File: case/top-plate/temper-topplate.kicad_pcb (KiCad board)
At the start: 2 copper layers, 111.4 x 90 mm, 21 parts, among them SW10 SW_PUSH, SW11 SW_PUSH, SW12 SW_PUSH, SW14 SW_PUSH, SW15 SW_PUSH, SW16 SW_PUSH, SW17 SW_PUSH, SW18 SW_PUSH, SW19 SW_PUSH, SW2 SW_PUSH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

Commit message: fix: save plate modification
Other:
- rule pad_to_mask_clearance: 0.2 -> 0
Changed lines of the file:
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@@
 			(dielectric_constraints no)
 		)
-		(pad_to_mask_clearance 0.2)
-		(solder_mask_min_width 0.1)
+		(pad_to_mask_clearance 0)
 		(allow_soldermask_bridges_in_footprints no)
 		(aux_axis_origin 145.73 12.66)
@@
 			(psnegative no)
 			(psa4output no)
-			(plotreference yes)
-			(plotvalue yes)
-			(plotfptext yes)
+			(plotreference no)
+			(plotvalue no)
+			(plotfptext no)
 			(plotinvisibletext no)
 			(sketchpadsonfab no)

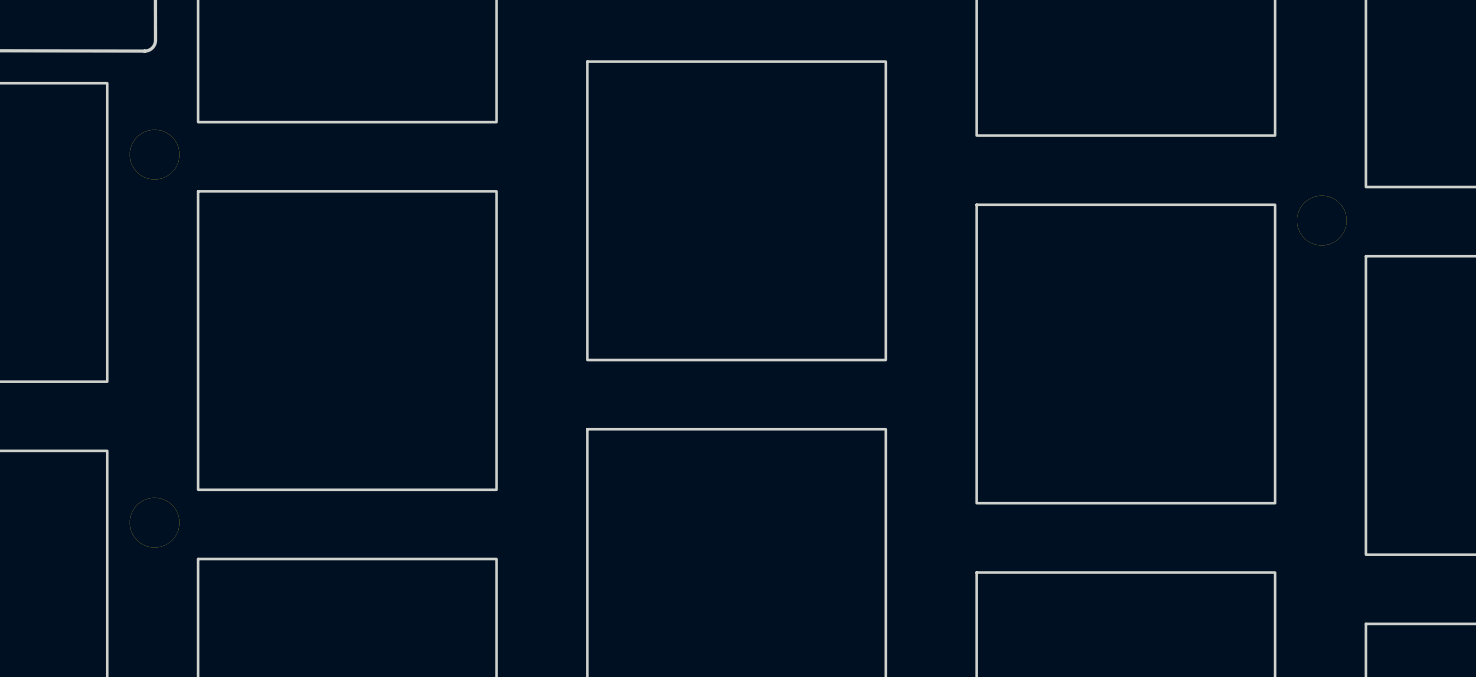
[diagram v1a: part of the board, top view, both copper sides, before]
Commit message: feat: remove useless holes from top plate
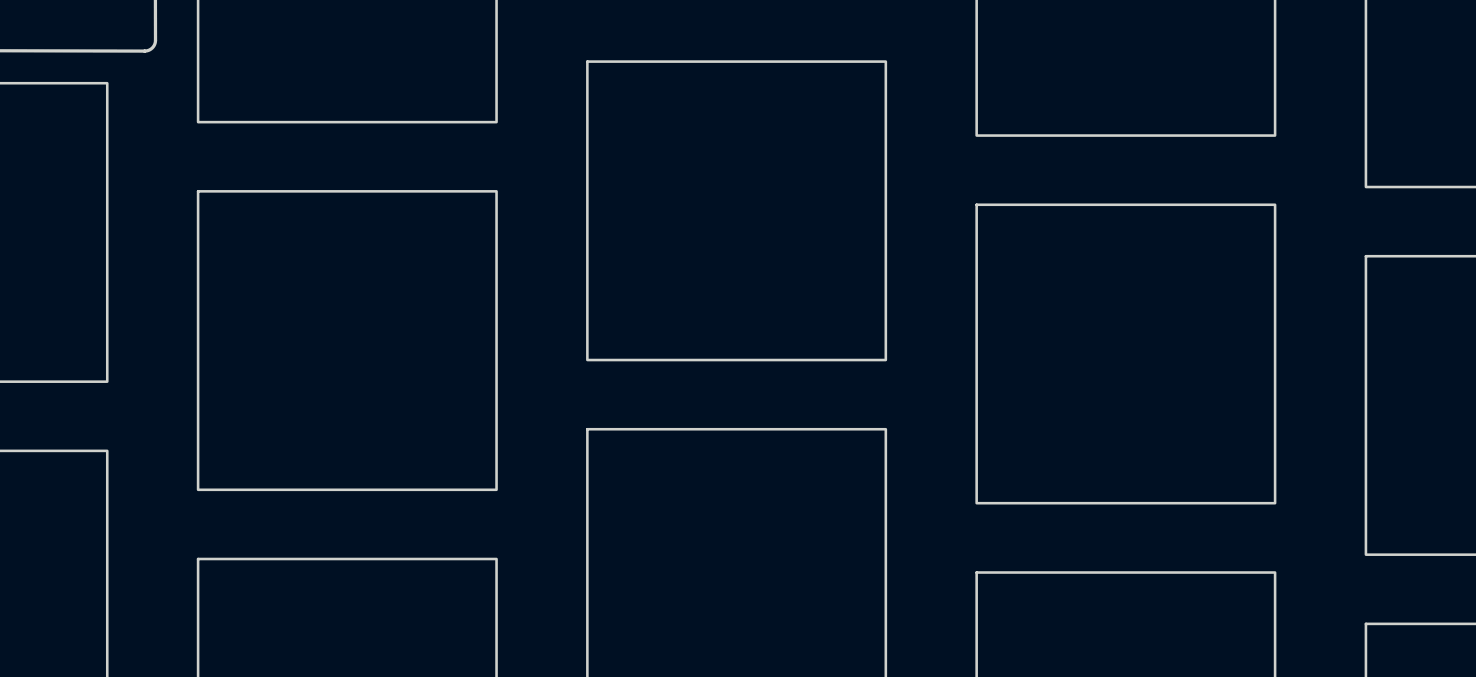
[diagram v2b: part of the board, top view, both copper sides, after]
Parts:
- removed h5: h5, kbd:M2_Threads_v2
- removed h6: h6, kbd:M2_Threads_v2
- removed h7: h7, kbd:M2_Threads_v2
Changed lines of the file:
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@@
 			(drillshape 0)
 			(scaleselection 1)
-			(outputdirectory "gerber-plate/")
+			(outputdirectory "out/")
 		)
 	)
@@
 		)
 	)
-	(footprint "kbd:M2_Threads_v2"
-		(layer "F.Cu")
-		(at 95 66.802)
-		(descr "Mounting Hole 2.2mm, no annular, M2")
-		(tags "mounting hole 2.2mm no annular m2")
-		(property "Reference" "h6"
-			(at -0.95 -0.55 0)
-			(layer "F.Fab")
-			(hide yes)
-			(effects
-				(font
-					(size 1 1)
-					(thickness 0.15)
-				)
-			)
-		)
-		(property "Value" "h6"
-			(at 0 0.55 0)
-			(layer "F.Fab")
-			(hide yes)
-			(effects
-				(font
-					(size 1 1)
-					(thickness 0.15)
-				)
-			)
-		)
-		(property "Footprint" ""
-			(at 0 0 0)
-			(unlocked yes)
-			(layer "F.Fab")
-			(hide yes)
-			(effects
-				(font
-					(size 1.27 1.27)
-				)
-			)
-		)
-		(property "Datasheet" ""
-			(at 0 0 0)
-			(unlocked yes)
-			(layer "F.Fab")
-			(hide yes)
-			(effects
-				(font
-					(size 1.27 1.27)
-				)
-			)
-		)
-		(property "Description" ""
-			(at 0 0 0)
-			(unlocked yes)
-			(layer "F.Fab")
-			(hide yes)
-			(effects
-				(font
-					(size 1.27 1.27)
-				)
-			)
-		)
-		(attr exclude_from_pos_files exclude_from_bom)
-		(fp_text user "${REFERENCE}"
-			(at 0.3 0 0)
-			(layer "F.Fab")
-			(effects
-				(font
-					(size 1 1)
-					(thickness 0.15)
-				)
-			)
-		)
-		(pad "" thru_hole circle
-			(at 0 0)
-			(size 2.3 2.3)
-			(drill 2.3)
-			(layers "*.Cu" "*.Mask")
-			(remove_unused_layers no)
-		)
-	)
-	(footprint "kbd:M2_Threads_v2"
-		(layer "F.Cu")
-		(at 148.971 69.85)
-		(descr "Mounting Hole 2.2mm, no annular, M2")
-		(tags "mounting hole 2.2mm no annular m2")
-		(property "Reference" "h7"
-			(at -0.95 -0.55 0)
-			(layer "F.Fab")
-			(hide yes)
-			(effects
-				(font
-					(size 1 1)
-					(thickness 0.15)
-				)
-			)
-		)
-		(property "Value" "h7"
-			(at 0 0.55 0)
-			(layer "F.Fab")
-			(hide yes)
-			(effects
-				(font
-					(size 1 1)
-					(thickness 0.15)
-				)
-			)
-		)
-		(property "Footprint" ""
-			(at 0 0 0)
-			(unlocked yes)
-			(layer "F.Fab")
-			(hide yes)
-			(effects
-				(font
-					(size 1.27 1.27)
-				)
-			)
-		)
-		(property "Datasheet" ""
-			(at 0 0 0)
-			(unlocked yes)
-			(layer "F.Fab")
-			(hide yes)
-			(effects
-				(font
-					(size 1.27 1.27)
-				)
-			)
-		)
-		(property "Description" ""
-			(at 0 0 0)
-			(unlocked yes)
-			(layer "F.Fab")
-			(hide yes)
-			(effects
-				(font
-					(size 1.27 1.27)
-				)
-			)
-		)
-		(attr exclude_from_pos_files exclude_from_bom)
-		(fp_text user "${REFERENCE}"
-			(at 0.127 0 0)
-			(layer "F.Fab")
-			(effects
-				(font
-					(size 1 1)
-					(thickness 0.15)
-				)
-			)
-		)
-		(pad "" thru_hole circle
-			(at 0 0)
-			(size 2.3 2.3)
-			(drill 2.3)
-			(layers "*.Cu" "*.Mask")
-			(remove_unused_layers no)
-		)
-	)
-	(footprint "kbd:M2_Threads_v2"
-		(layer "F.Cu")
-		(at 95 83.82)
-		(descr "Mounting Hole 2.2mm, no annular, M2")
-		(tags "mounting hole 2.2mm no annular m2")
-		(property "Reference" "h5"
-			(at -0.95 -0.55 0)
-			(layer "F.Fab")
-			(hide yes)
-			(effects
-				(font
-					(size 1 1)
-					(thickness 0.15)
-				)
-			)
-		)
-		(property "Value" "h5"
-			(at 0 0.55 0)
-			(layer "F.Fab")
-			(hide yes)
-			(effects
-				(font
-					(size 1 1)
-					(thickness 0.15)
-				)
-			)
-		)
-		(property "Footprint" ""
-			(at 0 0 0)
-			(unlocked yes)
-			(layer "F.Fab")
-			(hide yes)
-			(effects
-				(font
-					(size 1.27 1.27)
-				)
-			)
-		)
-		(property "Datasheet" ""
-			(at 0 0 0)
-			(unlocked yes)
-			(layer "F.Fab")
-			(hide yes)
-			(effects
-				(font
-					(size 1.27 1.27)
-				)
-			)
-		)
-		(property "Description" ""
-			(at 0 0 0)
-			(unlocked yes)
-			(layer "F.Fab")
-			(hide yes)
-			(effects
-				(font
-					(size 1.27 1.27)
-				)
-			)
-		)
-		(attr exclude_from_pos_files exclude_from_bom)
-		(fp_text user "${REFERENCE}"
-			(at 0.3 0 0)
-			(layer "F.Fab")
-			(effects
-				(font
-					(size 1 1)
-					(thickness 0.15)
-				)
-			)
-		)
-		(pad "" thru_hole circle
-			(at 0 0)
-			(size 2.3 2.3)
-			(drill 2.3)
-			(layers "*.Cu" "*.Mask")
-			(remove_unused_layers no)
-		)
-	)
